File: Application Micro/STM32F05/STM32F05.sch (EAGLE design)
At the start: 17 parts, among them Q1 ASF

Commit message: Changes 11/18/2015
Continued schematic design.
Created PCB file
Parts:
- added D1: (no value), DiscreteComponents:DIODE-DO-214AC
- added RN1: (no value), DiscreteComponents:2R-NEXBV4V
- added SV1, SV2, SV3, SV4: (no value), con-lsta:FE08-2
- added T1: FDN340P, DiscreteComponents:FDN340P
- added U$4: MICROUSB, Other:MICROUSB
- C11: value (none) -> 0.1uF
- C7: value 0.01uF -> 10nF
- R1, R2: value (none) -> 10K
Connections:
- removed net N$24: U$1G$2.PB2
- net GND: now also U$1G$2.PB2
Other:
- note added: "Micro USB"
- note added: "Missing AP1117... Regulator"
- moved on the sheet: C11
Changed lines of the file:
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@@
 <part name="C5" library="rcl" deviceset="C-US" device="C0603" value="0.1uF"/>
 <part name="C6" library="rcl" deviceset="C-US" device="C0603" value="0.1uF"/>
-<part name="C7" library="rcl" deviceset="C-US" device="C0603" value="0.01uF"/>
+<part name="C7" library="rcl" deviceset="C-US" device="C0603" value="10nF"/>
 <part name="C8" library="rcl" deviceset="C-US" device="C0603" value="4.7uF"/>
 <part name="C9" library="rcl" deviceset="C-US" device="C0603" value="0.1uF"/>
 <part name="C10" library="rcl" deviceset="C-US" device="C0603" value="1uF"/>
 <part name="Q1" library="DiscreteComponents" deviceset="ASF*" device=""/>
-<part name="C11" library="rcl" deviceset="C-US" device="C0603"/>
+<part name="C11" library="rcl" deviceset="C-US" device="C0603" value="0.1uF"/>
 <part name="GND2" library="supply1" deviceset="GND" device=""/>
 <part name="U$2" library="DiscreteComponents" deviceset="SWITCH" device=""/>
 <part name="U$1" library="Other" deviceset="STM32F405" device=""/>
 <part name="U$3" library="DiscreteComponents" deviceset="SWITCH" device=""/>
-<part name="R1" library="rcl" deviceset="R-US_" device="R0603"/>
-<part name="R2" library="rcl" deviceset="R-US_" device="R0603"/>
+<part name="R1" library="rcl" deviceset="R-US_" device="R0603" value="10K"/>
+<part name="R2" library="rcl" deviceset="R-US_" device="R0603" value="10K"/>
 <part name="GND4" library="supply1" deviceset="GND" device=""/>
 <part name="GND5" library="supply1" deviceset="GND" device=""/>
@@
 <part name="+3V3" library="supply1" deviceset="+3V3" device=""/>
 <part name="+3V4" library="supply1" deviceset="+3V3" device=""/>
+<part name="GND3" library="supply1" deviceset="GND" device=""/>
+<part name="FRAME2" library="frames" deviceset="FRAME_A_L" device=""/>
+<part name="U$4" library="Other" deviceset="MICROUSB" device=""/>
+<part name="RN1" library="DiscreteComponents" deviceset="2R-N" device="EXBV4V"/>
+<part name="T1" library="DiscreteComponents" deviceset="FDN340P" device="" value="FDN340P"/>
+<part name="D1" library="DiscreteComponents" deviceset="DIODE-" device="DO-214AC"/>
+<part name="SV1" library="con-lsta" deviceset="FE08-2" device=""/>
+<part name="SV2" library="con-lsta" deviceset="FE08-2" device=""/>
+<part name="SV3" library="con-lsta" deviceset="FE08-2" device=""/>
+<part name="SV4" library="con-lsta" deviceset="FE08-2" device=""/>
 </parts>
 <sheets>
@@
 <text x="10.16" y="129.54" size="1.778" layer="95">One for each VDD</text>
 <text x="-20.32" y="129.54" size="1.778" layer="95">Conect to any one VDD</text>
+<text x="299.72" y="170.18" size="1.778" layer="95">Micro USB</text>
+<text x="373.38" y="106.68" size="1.778" layer="95">Missing AP1117... Regulator</text>
 </plain>
 <instances>
@@
 <instance part="C10" gate="G$1" x="45.72" y="109.22"/>
 <instance part="Q1" gate="G$1" x="86.36" y="180.34"/>
-<instance part="C11" gate="G$1" x="167.64" y="119.38"/>
+<instance part="C11" gate="G$1" x="167.64" y="116.84"/>
 <instance part="GND2" gate="1" x="68.58" y="170.18"/>
 <instance part="U$2" gate="G$1" x="177.8" y="177.8"/>
@@
 <instance part="+3V3" gate="G$1" x="162.56" y="142.24"/>
 <instance part="+3V4" gate="G$1" x="68.58" y="193.04"/>
+<instance part="GND3" gate="1" x="5.08" y="177.8"/>
+<instance part="FRAME2" gate="G$1" x="261.62" y="-15.24"/>
+<instance part="FRAME2" gate="G$2" x="431.8" y="-15.24"/>
+<instance part="U$4" gate="G$1" x="304.8" y="160.02"/>
+<instance part="RN1" gate="A" x="342.9" y="165.1"/>
+<instance part="RN1" gate="B" x="342.9" y="160.02"/>
+<instance part="T1" gate="A" x="358.14" y="139.7" rot="MR270"/>
+<instance part="D1" gate="G$1" x="383.54" y="157.48" rot="R270"/>
+<instance part="SV1" gate="G$1" x="302.26" y="119.38"/>
+<instance part="SV2" gate="G$1" x="327.66" y="119.38"/>
+<instance part="SV3" gate="G$1" x="302.26" y="83.82"/>
+<instance part="SV4" gate="G$1" x="327.66" y="83.82"/>
 </instances>
 <busses>
@@
 <wire x1="177.8" y1="106.68" x2="172.72" y2="106.68" width="0.1524" layer="91"/>
 <wire x1="172.72" y1="106.68" x2="167.64" y2="106.68" width="0.1524" layer="91"/>
-<wire x1="167.64" y1="106.68" x2="167.64" y2="114.3" width="0.1524" layer="91"/>
+<wire x1="167.64" y1="106.68" x2="167.64" y2="111.76" width="0.1524" layer="91"/>
 <wire x1="172.72" y1="106.68" x2="172.72" y2="104.14" width="0.1524" layer="91"/>
 <junction x="172.72" y="106.68"/>
 <pinref part="GND5" gate="1" pin="GND"/>
+</segment>
+<segment>
+<pinref part="U$1" gate="G$2" pin="PB2"/>
+<wire x1="15.24" y1="182.88" x2="5.08" y2="182.88" width="0.1524" layer="91"/>
+<wire x1="5.08" y1="182.88" x2="5.08" y2="180.34" width="0.1524" layer="91"/>
+<pinref part="GND3" gate="1" pin="GND"/>
 </segment>
 </net>
@@
 <junction x="162.56" y="124.46"/>
 <pinref part="C11" gate="G$1" pin="1"/>
-<wire x1="167.64" y1="124.46" x2="167.64" y2="121.92" width="0.1524" layer="91"/>
+<wire x1="167.64" y1="124.46" x2="167.64" y2="119.38" width="0.1524" layer="91"/>
 <junction x="167.64" y="124.46"/>
 </segment>
@@
 </segment>
 </net>
-<net name="N$24" class="0">
-<segment>
-<pinref part="U$1" gate="G$2" pin="PB2"/>
-<wire x1="15.24" y1="182.88" x2="10.16" y2="182.88" width="0.1524" layer="91"/>
-</segment>
-</net>

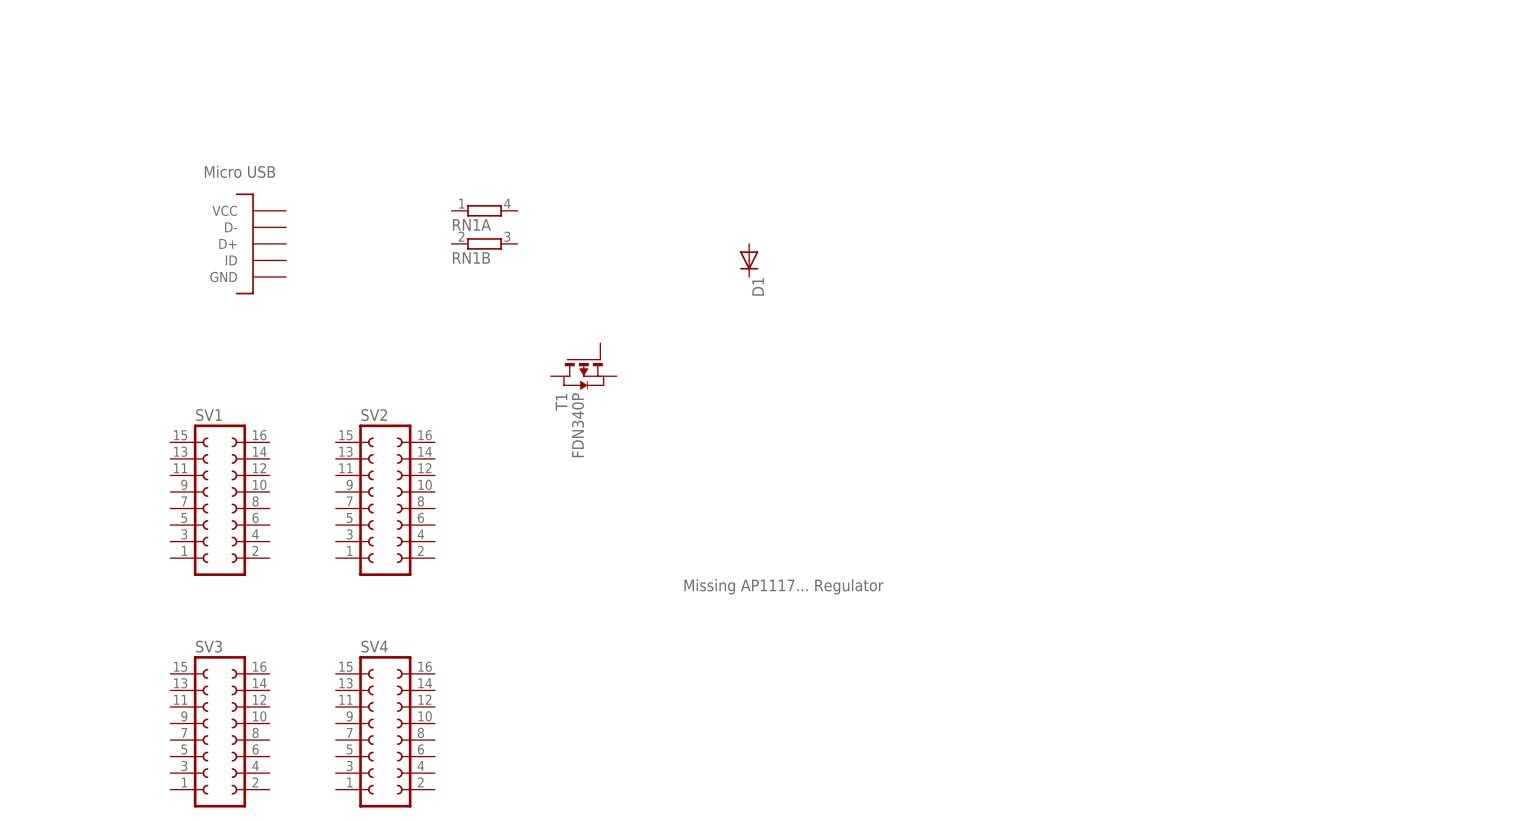
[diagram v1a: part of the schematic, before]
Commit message: Updated application micro board
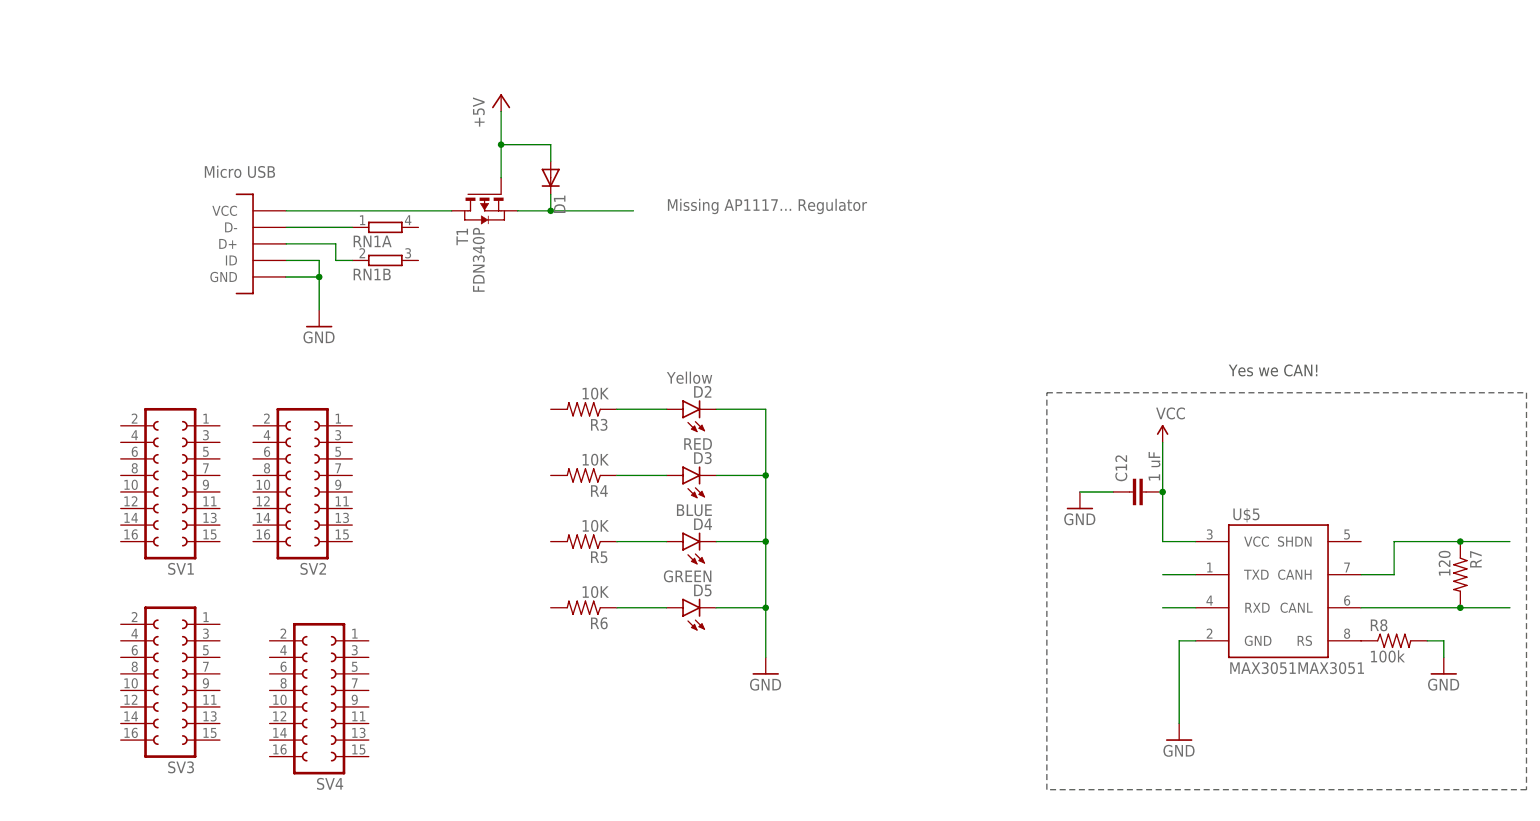
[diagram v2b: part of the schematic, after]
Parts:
- added C12: 1 uF, capacitor-wima:C2,5-3
- added D2: Yellow, SparkFun-LED:LED-YELLOW0603
- added D3: RED, SparkFun-LED:LED-RED0603
- added D4: BLUE, SparkFun-LED:LED-BLUE0603
- added D5: GREEN, SparkFun-LED:LED-GREEN0603
- added R3, R4, R5, R6: 10K, rcl:R-US_R0603
- added R7: 120, resistor:R-US_0204/2V
- added R8: 100k, resistor:R-US_0204/2V
- added U$5: MAX3051MAX3051, MAX3051 Library:MAX3051MAX3051
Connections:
- new net +5V: D1.A, T1.G
- new net CANH: R7.1, U$5.CANH
- new net CANL: R7.2, U$5.CANL
- new net N$24: RN1B.1, U$4.D+
- new net N$56: RN1A.1, U$4.D-
- new net N$57: T1.D, U$4.VCC
- new net N$58: D1.C, T1.S
- new net N$59: D2.A, R3.1
- new net N$60: D3.A, R4.1
- new net N$61: D4.A, R5.1
- new net N$62: D5.A, R6.1
- new net N$63: R8.1, U$5.RS
- new net RXD: U$5.RXD
- new net TXD: U$5.TXD
- new net VCC: C12.2, U$5.VCC
- net GND: now also C12.1, D2.C, D3.C, D4.C, D5.C, R8.2, U$4.GND, U$4.ID, U$5.GND
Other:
- note added: "Yes we CAN!"
- moved on the sheet: D1, RN1A, RN1B, SV1, SV2, SV3, SV4, T1

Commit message: Continued work on application micro
Added circuitry for bi-directional linear regulator. Named some pins.
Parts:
- removed C12: 1 uF, capacitor-wima:C2,5-3
- removed R7: 120, resistor:R-US_0204/2V
- removed R8: 100k, resistor:R-US_0204/2V
- added BSS138: n-chanel mosfet, DiscreteComponents:BSS138
- added C13: 0.1uF, rcl:C-USC0603
- added R10, R11, R12, R9: 10K, rcl:R-US_R0603
- added R13: 120, rcl:R-US_R0603
- added R14: 100K, rcl:R-US_R0603
- added U$6: BSS138, DiscreteComponents:BSS138
- ASV: value ASF -> 8.000MHZ
- SV1: value (none) -> Left
- SV2: value (none) -> Top
- SV3: value (none) -> Bottom
- SV4: value (none) -> Right
- renumbered Q1 to ASV
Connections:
- removed net N$1: C1.1, U$1G$4.VCAP_1
- removed net N$10: U$1G$1.PA2
- removed net N$11: U$1G$1.PA3
- removed net N$12: U$1G$1.PA4
- removed net N$13: U$1G$1.PA5
- removed net N$14: U$1G$1.PA6
- removed net N$15: U$1G$1.PA7
- removed net N$16: U$1G$1.PA8
- removed net N$17: U$1G$1.PA9
- removed net N$18: U$1G$1.PA10
- removed net N$19: U$1G$1.PA11
- removed net N$2: C2.1, U$1G$4.VCAP_2
- removed net N$20: U$1G$1.PA12
- removed net N$21: U$1G$1.PA13
- removed net N$22: U$1G$1.PA14
- removed net N$23: U$1G$1.PA15
- removed net N$25: U$1G$2.PB3
- removed net N$26: U$1G$2.PB4
- removed net N$27: U$1G$2.PB5
- removed net N$28: U$1G$2.PB6
- removed net N$29: U$1G$2.PB7
- removed net N$3: ASV.FO, U$1G$7.PH0_OSCIN
- removed net N$30: U$1G$2.PB8
- removed net N$31: U$1G$2.PB9
- removed net N$32: U$1G$2.PB10
- removed net N$33: U$1G$2.PB11
- removed net N$34: U$1G$2.PB12
- removed net N$35: U$1G$2.PB13
- removed net N$36: U$1G$2.PB14
- removed net N$37: U$1G$2.PB15
- removed net N$38: U$1G$3.PC0
- removed net N$39: U$1G$3.PC1
- removed net N$4: C11.1, R2.1, U$1G$6.NRST, U$3.P$1
- removed net N$40: U$1G$3.PC2
- removed net N$41: U$1G$3.PC3
- removed net N$42: U$1G$3.PC4
- removed net N$43: U$1G$3.PC5
- removed net N$44: U$1G$3.PC6
- removed net N$45: U$1G$3.PC7
- removed net N$46: U$1G$3.PC8
- removed net N$47: U$1G$3.PC9
- removed net N$48: U$1G$3.PC10
- removed net N$49: U$1G$3.PC11
- removed net N$5: R1.2, U$1G$5.BOOT0, U$2.P$1
- removed net N$50: U$1G$3.PC12
- removed net N$51: U$1G$3.PC13
- removed net N$52: U$1G$3.PC14
- removed net N$53: U$1G$3.PC15
- removed net N$54: U$1G$8.PD2
- removed net N$55: U$1G$7.PH1_OSCOUT
- removed net N$6: U$1G$1.PA0_WKUP
- removed net N$7: U$1G$1.PA1
- removed net N$8: U$1G$2.PB0
- removed net N$9: U$1G$2.PB1
- removed net VCC: C12.2, U$5.VCC
- new net BOOT0: R1.2, SV2.12, U$1G$5.BOOT0, U$2.P$1
- new net NRST: C11.1, R2.1, SV1.7, U$1G$6.NRST, U$3.P$1
- new net OSCIN: ASV.FO, SV1.5, U$1G$7.PH0_OSCIN
- new net OSCOUT: SV1.6, U$1G$7.PH1_OSCOUT
- new net PIN10: SV1.10, U$1G$3.PC2
- new net PIN11: SV1.11, U$1G$3.PC3
- new net PIN14: SV1.14, U$1G$1.PA0_WKUP
- new net PIN15: SV1.15, U$1G$1.PA1
- new net PIN16: SV1.16, U$1G$1.PA2
- new net PIN17: SV3.1, U$1G$1.PA3
- new net PIN2: SV1.2, U$1G$3.PC13
- new net PIN20: SV3.4, U$1G$1.PA4
- new net PIN21: SV3.5, U$1G$1.PA5
- new net PIN22: SV3.6, U$1G$1.PA6
- new net PIN23: SV3.7, U$1G$1.PA7
- new net PIN24: SV3.8, U$1G$3.PC4
- new net PIN25: SV3.9, U$1G$3.PC5
- new net PIN26: SV3.10, U$1G$2.PB0
- new net PIN27: SV3.11, U$1G$2.PB1
- new net PIN29: SV3.13, U$1G$2.PB10
- new net PIN3: SV1.3, U$1G$3.PC14
- new net PIN30: SV3.14, U$1G$2.PB11
- new net PIN33: SV4.1, U$1G$2.PB12
- new net PIN34: SV4.2, U$1G$2.PB13
- new net PIN35: SV4.3, U$1G$2.PB14
- new net PIN36: SV4.4, U$1G$2.PB15
- new net PIN37: SV4.5, U$1G$3.PC6
- new net PIN38: SV4.6, U$1G$3.PC7
- new net PIN39: SV4.7, U$1G$3.PC8
- new net PIN4: SV1.4, U$1G$3.PC15
- new net PIN40: SV4.8, U$1G$3.PC9
- new net PIN41: SV4.9, U$1G$1.PA8
- new net PIN42: SV4.10, U$1G$1.PA9
- new net PIN43: SV4.11, U$1G$1.PA10
- new net PIN44: SV4.12, U$1G$1.PA11
- new net PIN45: SV4.13, U$1G$1.PA12
- new net PIN46: SV4.14, U$1G$1.PA13
- new net PIN49: SV2.1, U$1G$1.PA14
- new net PIN50: SV2.2, U$1G$1.PA15
- new net PIN51: SV2.3, U$1G$3.PC10
- new net PIN52: SV2.4, U$1G$3.PC11
- new net PIN53: SV2.5, U$1G$3.PC12
- new net PIN54: SV2.6, U$1G$8.PD2
- new net PIN55: SV2.7, U$1G$2.PB3
- new net PIN56: SV2.8, U$1G$2.PB4
- new net PIN57: SV2.9, U$1G$2.PB5
- new net PIN58: SV2.10, U$1G$2.PB6
- new net PIN59: SV2.11, U$1G$2.PB7
- new net PIN61: SV2.13, U$1G$2.PB8
- new net PIN62: SV2.14, U$1G$2.PB9
- new net PIN8: SV1.8, U$1G$3.PC0
- new net PIN9: SV1.9, U$1G$3.PC1
- new net SCL1: BSS138.S, R11.1
- new net SCL2: BSS138.D, R9.1
- new net SDA1: R12.1, U$6.S
- new net SDA2: R10.1, U$6.D
- new net VCAP_1: C1.1, SV3.15, U$1G$4.VCAP_1
- new net VCAP_2: C2.1, SV4.15, U$1G$4.VCAP_2
- net +3V3: now also BSS138.G, C13.1, R11.2, R12.2, SV1.1, SV1.13, SV2.16, SV3.16, SV3.3, SV4.16, U$5.VCC, U$6.G
- net +5V: now also R10.2, R9.2
- net CANH: now also R13.1; no longer R7.1
- net CANL: now also R13.2; no longer R7.2
- net GND: now also C13.2, R14.2, SV1.12, SV2.15, SV3.12, SV3.2; no longer C12.1, R8.2
- net N$63: now also R14.1; no longer R8.1
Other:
- note added: "Bi-Directional Level Shifter"
- moved on the sheet: SV1, SV2, SV3, SV4

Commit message: Added last parts to application board microcontroller.
Added the linear regulator, finished as much of schematic as we can for
now. *I think*  Now all that's left is deciding what pins do what.
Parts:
- added C12, C14: 0.22uF, rcl:C-USC0603
- added T2: AP1117_LIN_REG, PowerComponents:AP1117_LIN_REG
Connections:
- new net USBD+: RN1B.2
- new net USBD-: RN1A.2
- net +3V3: now also C14.1, SV1.14, T2.VOUT; no longer SV1.13
- net GND: now also C12.2, C14.2, SV1.11, T2.GND; no longer SV1.12
- net N$58: now also C12.1, T2.VIN
- net PIN10: now also SV1.9; no longer SV1.10
- net PIN11: now also SV1.12; no longer SV1.11
- net PIN14: now also SV1.13; no longer SV1.14
- net PIN15: now also SV1.16; no longer SV1.15
- net PIN16: now also SV1.15; no longer SV1.16
- net PIN9: now also SV1.10; no longer SV1.9
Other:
- note added: "Random LEDs"
- note removed: "Missing AP1117... Regulator"
- moved on the sheet: C13, D1, D2, D3, D4, D5, R10, R11, R12, R13, R14, R3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

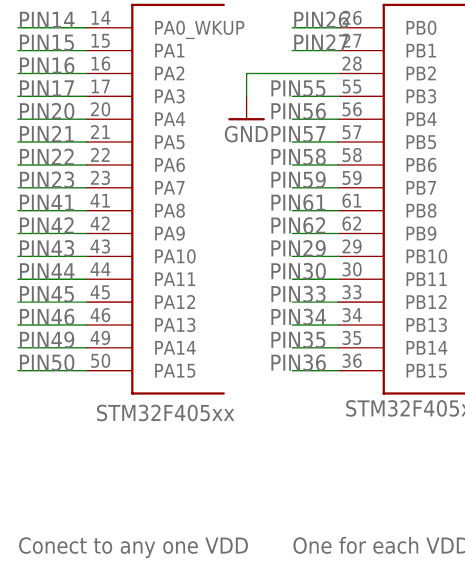
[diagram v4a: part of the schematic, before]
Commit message: Connected the programming pins
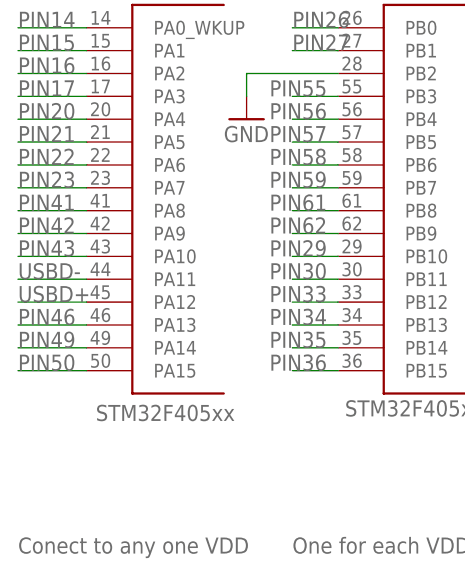
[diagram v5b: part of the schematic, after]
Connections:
- net PIN44: no longer U$1G$1.PA11
- net PIN45: no longer U$1G$1.PA12
- net USBD+: now also U$1G$1.PA12
- net USBD-: now also U$1G$1.PA11
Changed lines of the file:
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@@
 <net name="PIN44" class="0">
-<segment>
-<pinref part="U$1" gate="G$1" pin="PA11"/>
-<wire x1="-12.7" y1="160.02" x2="-20.32" y2="160.02" width="0.1524" layer="91"/>
-<label x="-20.32" y="160.02" size="1.778" layer="95"/>
-</segment>
 <segment>
 <pinref part="SV4" gate="G$1" pin="12"/>
@@
 </net>
 <net name="PIN45" class="0">
-<segment>
-<pinref part="U$1" gate="G$1" pin="PA12"/>
-<wire x1="-12.7" y1="157.48" x2="-20.32" y2="157.48" width="0.1524" layer="91"/>
-<label x="-20.32" y="157.48" size="1.778" layer="95"/>
-</segment>
 <segment>
 <pinref part="SV4" gate="G$1" pin="13"/>
@@
 <label x="327.66" y="137.16" size="1.778" layer="95"/>
 </segment>
+<segment>
+<pinref part="U$1" gate="G$1" pin="PA11"/>
+<wire x1="-12.7" y1="160.02" x2="-20.32" y2="160.02" width="0.1524" layer="91"/>
+<label x="-20.32" y="160.02" size="1.778" layer="95"/>
+</segment>
 </net>
 <net name="USBD+" class="0">
@@
 <label x="327.66" y="132.08" size="1.778" layer="95"/>
 </segment>
-</net>
+<segment>
+<pinref part="U$1" gate="G$1" pin="PA12"/>
+<wire x1="-12.7" y1="157.48" x2="-20.32" y2="157.48" width="0.1524" layer="91"/>
+<label x="-20.32" y="157.48" size="1.778" layer="95"/>
+</segment>
+</net>
